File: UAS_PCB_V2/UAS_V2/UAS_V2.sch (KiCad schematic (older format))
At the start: 19 parts, among them J1 UAS_PWR_IN, J2 UAS_JST-3-pin-Revised-Symbol, J3 UAS_JST-3-pin-Revised-Symbol, J4 UAS_SM07B-GHS-TB(LF)(SN), J5 UAS_SM04B-GHS-TB(LF)(SN)-, J6 UAS_SM04B-GHS-TB(LF)(SN)-, J7 UAS_SM07B-GHS-TB(LF)(SN), J8 UAS_SM08B-GHS-TB(LF)(SN), J9 UAS_SM08B-GHS-TB(LF)(SN), U1 UAS-rescue_5A-5V-Converter-UA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

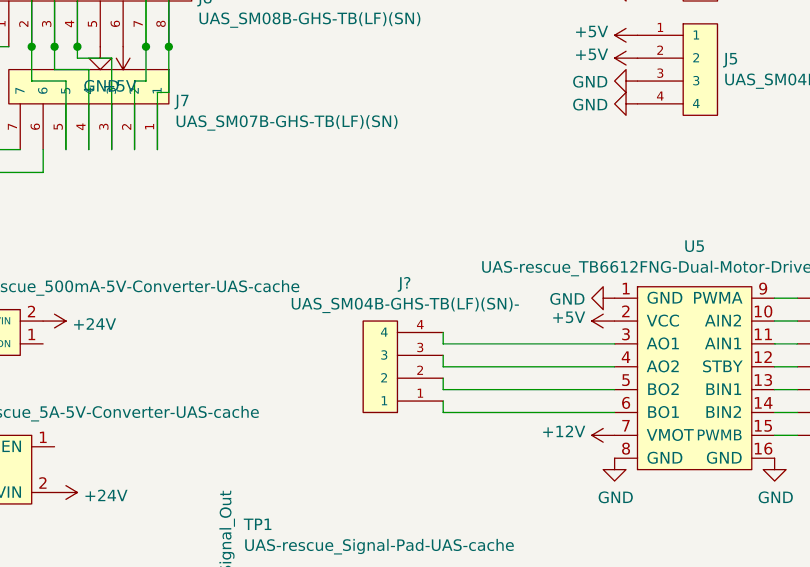
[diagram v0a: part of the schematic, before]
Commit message: footprint file system fixes
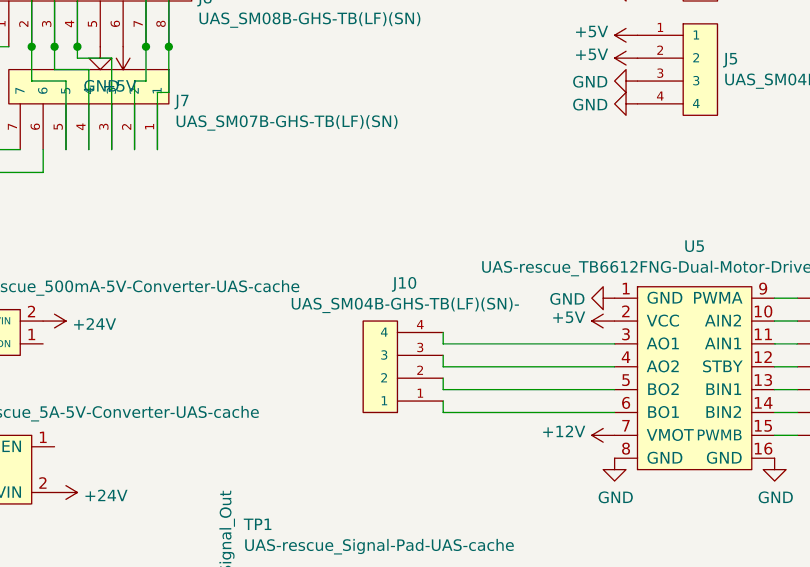
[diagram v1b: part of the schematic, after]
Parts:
- J4, J7: footprint JST_SM07B-GHS-TB(LF)(SN) -> UAS_V2:JST_SM08B-GHS-TB(LF)(SN)
- J5, J6: footprint JST_SM04B-GHS-TB(LF)(SN)- -> UAS_V2:JST_SM04B-GHS-TB(LF)(SN)-
- U4: footprint (none) -> UAS_V2:Pololu_12V_Step_Down_Regulator
- U5: footprint (none) -> UAS_V2:Pololu_TB6612_Dual_Motor_Driver_Carrier_SMT
- gave numbers to parts that had none: 1

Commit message: finalized merge
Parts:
- J2, J3: footprint (none) -> UAS_V2:MOLEX_SHDRRA3W50P0X200_1X3_0353630360
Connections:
- net at U5.3 (AO1): now also J10.1; no longer J10.4
- net at U5.4 (AO2): now also J10.2; no longer J10.3
- net at U5.5 (BO2): now also J10.3; no longer J10.2
- net at U5.6 (BO1): now also J10.4; no longer J10.1
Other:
- moved on the sheet: J10
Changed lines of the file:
@@
 F 0 "J2" H 3650 4850 50  0000 C CNN
 F 1 "UAS_JST-3-pin-Revised-Symbol" H 3417 4626 50  0000 C CNN
-F 2 "" H 3500 5200 50  0001 C CNN
+F 2 "UAS_V2:MOLEX_SHDRRA3W50P0X200_1X3_0353630360" H 3500 5200 50  0001 C CNN
 F 3 "" H 3500 5200 50  0001 C CNN
 	1    3500 4850
@@
 F 0 "J3" H 3650 4450 50  0000 C CNN
 F 1 "UAS_JST-3-pin-Revised-Symbol" H 3417 4226 50  0000 C CNN
-F 2 "" H 3500 4800 50  0001 C CNN
+F 2 "UAS_V2:MOLEX_SHDRRA3W50P0X200_1X3_0353630360" H 3500 4800 50  0001 C CNN
 F 3 "" H 3500 4800 50  0001 C CNN
 	1    3500 4450
@@
 L UAS-Old:UAS_SM04B-GHS-TB(LF)(SN)- J10
 U 1 1 6080DEC5
-P 3600 3150
-F 0 "J10" H 3367 2835 50  0000 C CNN
-F 1 "UAS_SM04B-GHS-TB(LF)(SN)-" H 3367 2926 50  0000 C CNN
-F 2 "JST_SM04B-GHS-TB(LF)(SN)-" H 3600 3150 50  0001 L BNN
-F 3 "" H 3600 3150 50  0001 L BNN
-F 4 "NA" H 3600 3150 50  0001 L BNN "PARTREV"
-F 5 "Manufacturer Recommendations" H 3600 3150 50  0001 L BNN "STANDARD"
-F 6 "JHS" H 3600 3150 50  0001 L BNN "MANUFACTURER"
-	1    3600 3150
-	-1   0    0    1
-$EndComp
-Wire Wire Line
-	4750 3100 4000 3100
-Wire Wire Line
-	4000 3100 4000 3050
-Wire Wire Line
-	4750 3200 4000 3200
-Wire Wire Line
-	4000 3200 4000 3150
-Wire Wire Line
-	4750 3300 4000 3300
-Wire Wire Line
-	4000 3300 4000 3250
-Wire Wire Line
-	4750 3400 4000 3400
-Wire Wire Line
-	4000 3400 4000 3350
+P 3700 3350
+F 0 "J10" H 3467 3035 50  0000 C CNN
+F 1 "UAS_SM04B-GHS-TB(LF)(SN)-" H 3467 3126 50  0000 C CNN
+F 2 "JST_SM04B-GHS-TB(LF)(SN)-" H 3700 3350 50  0001 L BNN
+F 3 "" H 3700 3350 50  0001 L BNN
+F 4 "NA" H 3700 3350 50  0001 L BNN "PARTREV"
+F 5 "Manufacturer Recommendations" H 3700 3350 50  0001 L BNN "STANDARD"
+F 6 "JHS" H 3700 3350 50  0001 L BNN "MANUFACTURER"
+	1    3700 3350
+	-1   0    0    -1
+$EndComp
+Wire Wire Line
+	4100 3400 4100 3450
+Wire Wire Line
+	4100 3300 4100 3350
+Wire Wire Line
+	4100 3200 4100 3250
+Wire Wire Line
+	4100 3100 4100 3150
 $Comp
 L power:+5V #PWR0126
@@
 	0    1    1    0
 $EndComp
+Wire Wire Line
+	4100 3100 4750 3100
+Wire Wire Line
+	4100 3200 4750 3200
+Wire Wire Line
+	4750 3300 4100 3300
+Wire Wire Line
+	4100 3400 4750 3400
 $EndSCHEMATC
